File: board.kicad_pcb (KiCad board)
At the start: 2 copper layers, 96.3 x 46.3 mm, 38 parts, among them J0 Battery Pads, J1 Shard, J2 USB-Micro, SW0 RESET, SW1 UP, SW2 DOWN, SW3 LEFT, SW4 RIGHT, SW5 BTN_A, SW6 BTN_B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

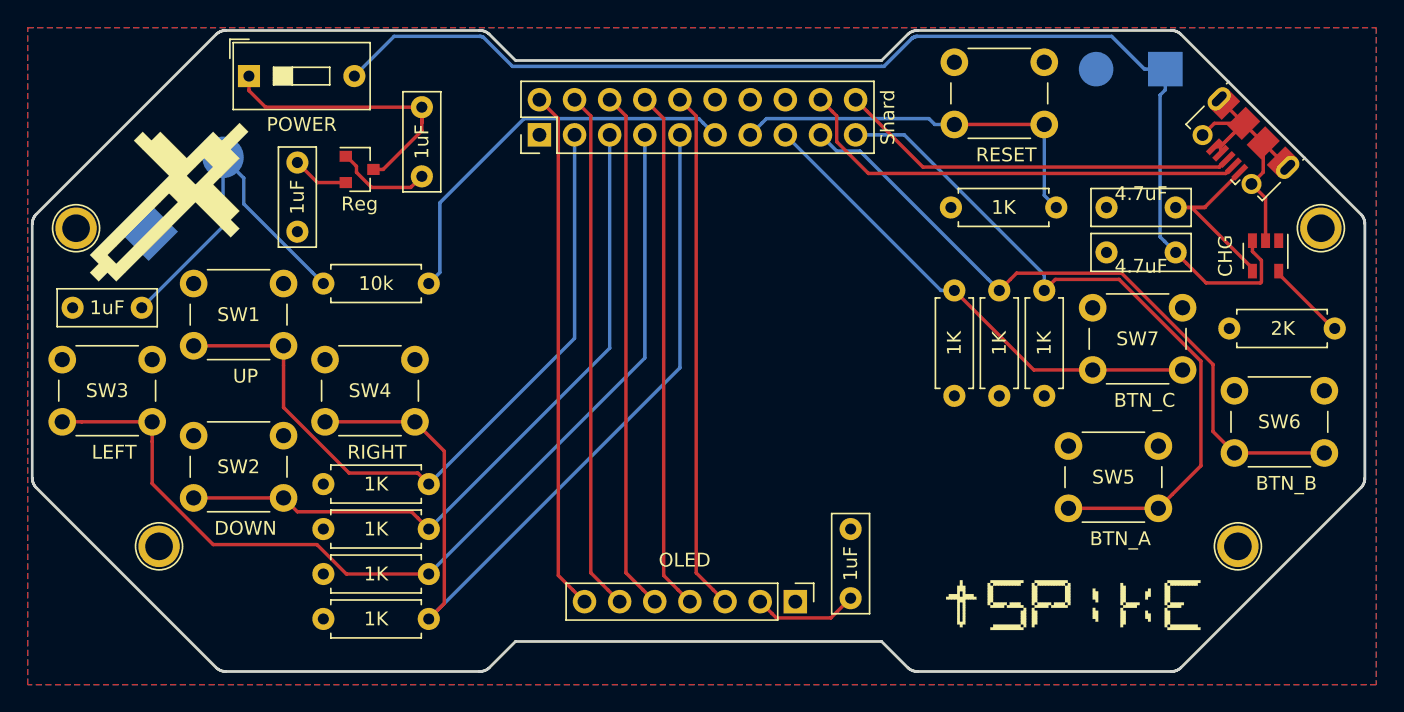
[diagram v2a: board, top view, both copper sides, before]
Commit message: board revised for mono oled
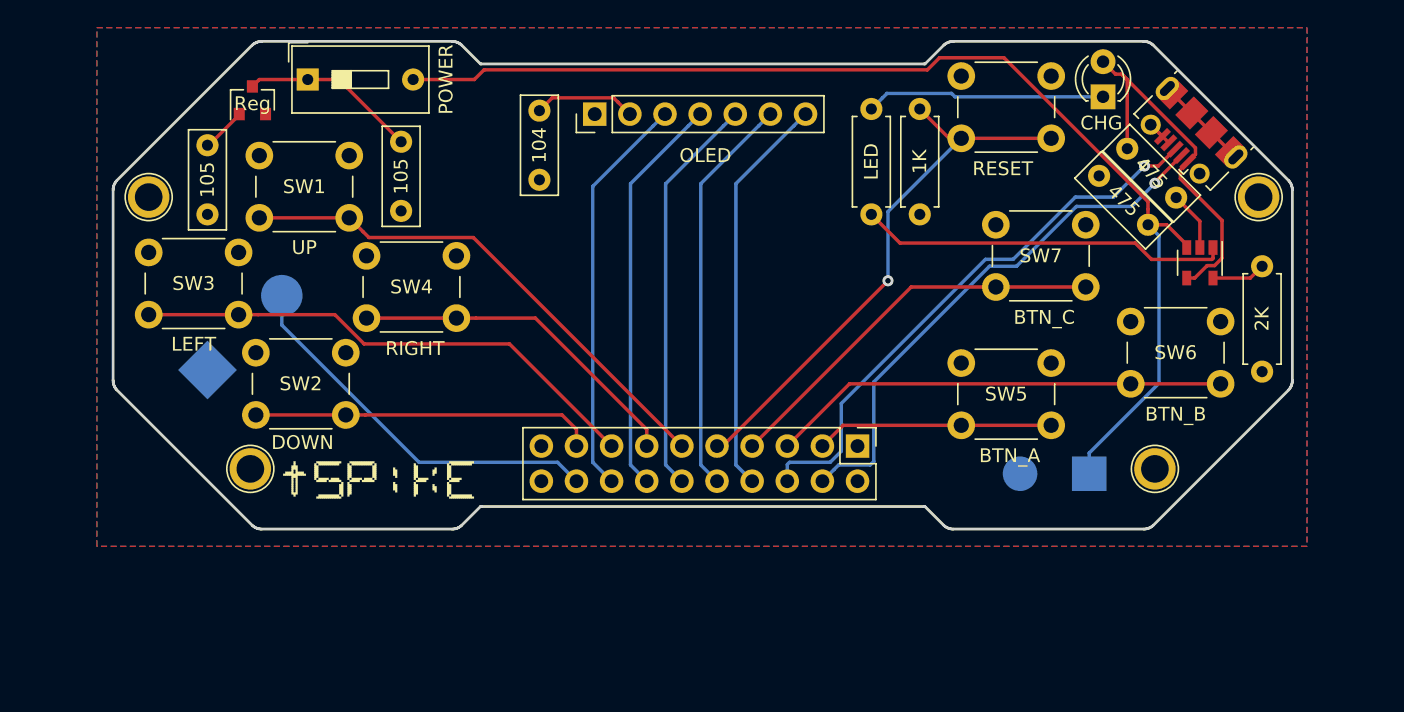
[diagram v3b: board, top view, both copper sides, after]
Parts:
- removed C4: 1uF, Capacitor_THT:C_Rect_L7.0mm_W2.5mm_P5.00mm
- removed R3, R4, R5, R6, R7: 1K, Resistor_THT:R_Axial_DIN0207_L6.3mm_D2.5mm_P7.62mm_Horizontal
- removed R8: 2K, Resistor_THT:R_Axial_DIN0207_L6.3mm_D2.5mm_P7.62mm_Horizontal
- removed R9: 10k, Resistor_THT:R_Axial_DIN0207_L6.3mm_D2.5mm_P7.62mm_Horizontal
- removed the REF** at (196.0, 97.0)
- removed the REF** at (106.0, 97.0)
- removed the REF** at (190.0, 120.0)
- removed the REF** at (112.0, 120.0)
- removed SPIKE: , SPIKE
- added D1: CHG, LED_THT:LED_D3.0mm, F.Cu at (180.2, 87.5)
- added REF**: TestPoint_Plated_Hole_D2.0mm, TestPoint:TestPoint_Plated_Hole_D2.0mm, F.Cu at (184.0, 114.4)
- added REF**: TestPoint_Plated_Hole_D2.0mm, TestPoint:TestPoint_Plated_Hole_D2.0mm, F.Cu at (111.2, 94.8)
- added REF**: TestPoint_Plated_Hole_D2.0mm, TestPoint:TestPoint_Plated_Hole_D2.0mm, F.Cu at (118.6, 114.4)
- added REF**: TestPoint_Plated_Hole_D2.0mm, TestPoint:TestPoint_Plated_Hole_D2.0mm, F.Cu at (191.5, 94.8)
- C1: value 1uF -> 104
- C2, C3: value 1uF -> 105
- C5, C6: value 4.7uF -> 475
- R1: value 1K -> LED
- R2: value 1K -> 2K
- U1: footprint Custom Footprints:128x128-OLED -> Custom Footprints:128x64-OLED
- U2: value CHG -> CHG CTRL
- moved R2 63.2 mm to (191.8, 99.8), turned to 270 degrees
- moved LOGO 48.6 mm to (120.7, 113.7)
- moved C1 41.8 mm to (139.5, 88.5), turned to 270 degrees
- moved U1 38.1 mm to (143.5, 88.8), turned to 90 degrees
- moved R1 37.5 mm to (163.5, 96.0), turned to 90 degrees
- moved J1 32.2 mm to (162.5, 112.8), turned to 270 degrees
- moved J0 29.8 mm to (176.8, 114.8)
- moved LS1 10.9 mm to (115.5, 107.2)
- moved SW1 10.4 mm to (119.2, 91.8)
- moved SW3 9.96 mm to (111.2, 98.8)
- moved SW5 9.80 mm to (170.0, 106.8)
- moved U3 9.22 mm to (118.8, 87.8), turned to 90 degrees
- moved SW7 9.22 mm to (172.5, 96.8)
- moved SW6 9.01 mm to (182.2, 103.8)
- moved SW4 8.08 mm to (127.0, 99.0)
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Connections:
- J1 pad 10: D_SCK -> D_DC
- J1 pad 11: SND -> UP
- J1 pad 12: GND -> D_RST
- J1 pad 13: RESET -> RIGHT
- J1 pad 14: GND -> D_MOSI
- J1 pad 15: BTN_C -> LEFT
- J1 pad 16: GND -> D_SCK
- J1 pad 17: BTN_B -> DOWN
- J1 pad 18: D- -> SND
- J1 pad 19: BTN_A -> GND
- J1 pad 2: D_CS -> GND
- J1 pad 20: D+ -> +3V3
- J1 pad 3: UP -> BTN_A
- J1 pad 4: D_DC -> D-
- J1 pad 5: DOWN -> BTN_B
- J1 pad 6: D_RST -> D+
- J1 pad 7: LEFT -> BTN_C
- J1 pad 8: D_MOSI -> D_CS
- J1 pad 9: RIGHT -> RESET
- LS1 pad 2: Net-(C4-Pad1) -> SND
- R1 pad 1: UP -> Net-(R1-Pad1)
- R1 pad 2: GND -> Net-(D1-Pad1)
- R2 pad 1: DOWN -> Net-(R2-Pad1)
- U2 pad 1: Net-(U2-Pad1) -> Net-(R1-Pad1)
- U2 pad 5: Net-(R8-Pad1) -> Net-(R2-Pad1)
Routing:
- net RIGHT: track 64.6 -> 24.8 mm
- net LEFT: track 71.9 -> 37.4 mm
- net BTN_A: track 51.5 -> 17.2 mm
- net DOWN: track 51.8 -> 24.8 mm
- net Net-(R1-Pad1): track 0.00 -> 26.9 mm
- net Net-(C4-Pad1): track 25.4 -> 0.00 mm
- net Net-(D1-Pad1): track 0.00 -> 17.3 mm
- net BTN_B: track 49.8 -> 33.2 mm
- net UP: track 53.4 -> 37.4 mm
- net CHARGE: track 14.3 -> 27.6 mm
- net GND: track 30.2 -> 17.0 mm
- net RESET: track 28.3 -> 40.2 mm, vias 0 -> 1
- net D+: track 29.1 -> 40.7 mm, vias 0 -> 1
- net D_DC: track 37.6 -> 29.1 mm
- net D_MOSI: track 37.6 -> 29.1 mm
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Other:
- board size 96.3 x 46.3 mm -> 85.3 x 35.3 mm

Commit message: swapped buttons to pull to GND
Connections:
- SW1 pad 1: +3V3 -> GND
- SW2 pad 1: +3V3 -> GND
- SW3 pad 1: +3V3 -> GND
- SW4 pad 1: +3V3 -> GND
- SW5 pad 1: +3V3 -> GND
- SW6 pad 1: +3V3 -> GND
- SW7 pad 1: +3V3 -> GND
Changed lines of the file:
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@@
     )
     (pad 1 thru_hole circle (at 6.5 0 90) (size 2 2) (drill 1.1) (layers *.Cu *.Mask)
-      (net 1 +3V3))
+      (net 2 GND))
     (pad 2 thru_hole circle (at 6.5 4.5 90) (size 2 2) (drill 1.1) (layers *.Cu *.Mask)
       (net 8 UP))
     (pad 1 thru_hole circle (at 0 0 90) (size 2 2) (drill 1.1) (layers *.Cu *.Mask)
-      (net 1 +3V3))
+      (net 2 GND))
     (pad 2 thru_hole circle (at 0 4.5 90) (size 2 2) (drill 1.1) (layers *.Cu *.Mask)
       (net 8 UP))
@@
       (net 9 DOWN))
     (pad 1 thru_hole circle (at 0 0 90) (size 2 2) (drill 1.1) (layers *.Cu *.Mask)
-      (net 1 +3V3))
+      (net 2 GND))
     (pad 2 thru_hole circle (at 6.5 4.5 90) (size 2 2) (drill 1.1) (layers *.Cu *.Mask)
       (net 9 DOWN))
     (pad 1 thru_hole circle (at 6.5 0 90) (size 2 2) (drill 1.1) (layers *.Cu *.Mask)
-      (net 1 +3V3))
+      (net 2 GND))
     (model ${KISYS3DMOD}/Button_Switch_THT.3dshapes/SW_PUSH_6mm.wrl
       (at (xyz 0 0 0))
@@
     )
     (pad 1 thru_hole circle (at 6.5 0 90) (size 2 2) (drill 1.1) (layers *.Cu *.Mask)
-      (net 1 +3V3))
+      (net 2 GND))
     (pad 2 thru_hole circle (at 6.5 4.5 90) (size 2 2) (drill 1.1) (layers *.Cu *.Mask)
       (net 10 LEFT))
     (pad 1 thru_hole circle (at 0 0 90) (size 2 2) (drill 1.1) (layers *.Cu *.Mask)
-      (net 1 +3V3))
+      (net 2 GND))
     (pad 2 thru_hole circle (at 0 4.5 90) (size 2 2) (drill 1.1) (layers *.Cu *.Mask)
       (net 10 LEFT))
@@
       (net 11 RIGHT))
     (pad 1 thru_hole circle (at 0 0 90) (size 2 2) (drill 1.1) (layers *.Cu *.Mask)
-      (net 1 +3V3))
+      (net 2 GND))
     (pad 2 thru_hole circle (at 6.5 4.5 90) (size 2 2) (drill 1.1) (layers *.Cu *.Mask)
       (net 11 RIGHT))
     (pad 1 thru_hole circle (at 6.5 0 90) (size 2 2) (drill 1.1) (layers *.Cu *.Mask)
-      (net 1 +3V3))
+      (net 2 GND))
     (model ${KISYS3DMOD}/Button_Switch_THT.3dshapes/SW_PUSH_6mm.wrl
       (at (xyz 0 0 0))
@@
     )
     (pad 1 thru_hole circle (at 6.5 0 90) (size 2 2) (drill 1.1) (layers *.Cu *.Mask)
-      (net 1 +3V3))
+      (net 2 GND))
     (pad 2 thru_hole circle (at 6.5 4.5 90) (size 2 2) (drill 1.1) (layers *.Cu *.Mask)
       (net 12 BTN_A))
     (pad 1 thru_hole circle (at 0 0 90) (size 2 2) (drill 1.1) (layers *.Cu *.Mask)
-      (net 1 +3V3))
+      (net 2 GND))
     (pad 2 thru_hole circle (at 0 4.5 90) (size 2 2) (drill 1.1) (layers *.Cu *.Mask)
       (net 12 BTN_A))
@@
       (net 13 BTN_B))
     (pad 1 thru_hole circle (at 0 0 90) (size 2 2) (drill 1.1) (layers *.Cu *.Mask)
-      (net 1 +3V3))
+      (net 2 GND))
     (pad 2 thru_hole circle (at 6.5 4.5 90) (size 2 2) (drill 1.1) (layers *.Cu *.Mask)
       (net 13 BTN_B))
     (pad 1 thru_hole circle (at 6.5 0 90) (size 2 2) (drill 1.1) (layers *.Cu *.Mask)
-      (net 1 +3V3))
+      (net 2 GND))
     (model ${KISYS3DMOD}/Button_Switch_THT.3dshapes/SW_PUSH_6mm.wrl
       (at (xyz 0 0 0))
@@
     )
     (pad 1 thru_hole circle (at 6.5 0 90) (size 2 2) (drill 1.1) (layers *.Cu *.Mask)
-      (net 1 +3V3))
+      (net 2 GND))
     (pad 2 thru_hole circle (at 6.5 4.5 90) (size 2 2) (drill 1.1) (layers *.Cu *.Mask)
       (net 14 BTN_C))
     (pad 1 thru_hole circle (at 0 0 90) (size 2 2) (drill 1.1) (layers *.Cu *.Mask)
-      (net 1 +3V3))
+      (net 2 GND))
     (pad 2 thru_hole circle (at 0 4.5 90) (size 2 2) (drill 1.1) (layers *.Cu *.Mask)
       (net 14 BTN_C))
@@
   (gr_line (start 167.3735 85.1265) (end 167.3074 85.123) (layer Edge.Cuts) (width 0.2))
   (gr_line (start 168.75 83.75) (end 167.3735 85.1265) (layer Edge.Cuts) (width 0.2))
-  (via (at 164.7 100.8) (size 0.8) (drill 0.4) (layers F.Cu B.Cu) (net 6))
   (segment (start 144.864999 87.574999) (end 145.190001 87.900001) (width 0.25) (layer F.Cu) (net 1))
   (segment (start 145.190001 87.900001) (end 146.04 88.75) (width 0.25) (layer F.Cu) (net 1))
   (segment (start 140.425001 87.574999) (end 144.864999 87.574999) (width 0.25) (layer F.Cu) (net 1))
   (segment (start 139.5 88.5) (end 140.425001 87.574999) (width 0.25) (layer F.Cu) (net 1))
-  (via (at 183.25 92.5) (size 0.8) (drill 0.4) (layers F.Cu B.Cu) (net 20))
-  (via (at 184 93.75) (size 0.8) (drill 0.4) (layers F.Cu B.Cu) (net 21))
   (segment (start 188.082151 90.082062) (end 189.849918 91.849829) (width 0.25) (layer F.Cu) (net 2))
   (segment (start 185.324435 87.324346) (end 186.667938 88.667849) (width 0.25) (layer F.Cu) (net 2))
@@
   (segment (start 183.5 95.61863) (end 183.5 96.75) (width 0.25) (layer F.Cu) (net 5))
   (segment (start 167.549546 85.551508) (end 168.426055 84.674999) (width 0.25) (layer F.Cu) (net 5))
+  (via (at 164.7 100.8) (size 0.8) (drill 0.4) (layers F.Cu B.Cu) (net 6))
   (segment (start 169.12 90.5) (end 170 90.5) (width 0.25) (layer F.Cu) (net 6))
   (segment (start 167 88.38) (end 169.12 90.5) (width 0.25) (layer F.Cu) (net 6))
@@
   (segment (start 143.355001 93.974999) (end 147.730001 89.599999) (width 0.25) (layer B.Cu) (net 19))
   (segment (start 144.72 115.29) (end 143.355001 113.925001) (width 0.25) (layer B.Cu) (net 19))
+  (via (at 183.25 92.5) (size 0.8) (drill 0.4) (layers F.Cu B.Cu) (net 20))
   (segment (start 184.25 92.5) (end 183.25 92.5) (width 0.25) (layer F.Cu) (net 20))
   (segment (start 185.465856 91.284144) (end 184.25 92.5) (width 0.25) (layer F.Cu) (net 20))
@@
   (segment (start 181 94.75) (end 183.25 92.5) (width 0.25) (layer B.Cu) (net 20))
   (segment (start 178.25 94.75) (end 181 94.75) (width 0.25) (layer B.Cu) (net 20))
+  (via (at 184 93.75) (size 0.8) (drill 0.4) (layers F.Cu B.Cu) (net 21))
   (segment (start 184 93.669239) (end 184 93.75) (width 0.25) (layer F.Cu) (net 21))
   (segment (start 185.925476 91.743763) (end 184 93.669239) (width 0.25) (layer F.Cu) (net 21))

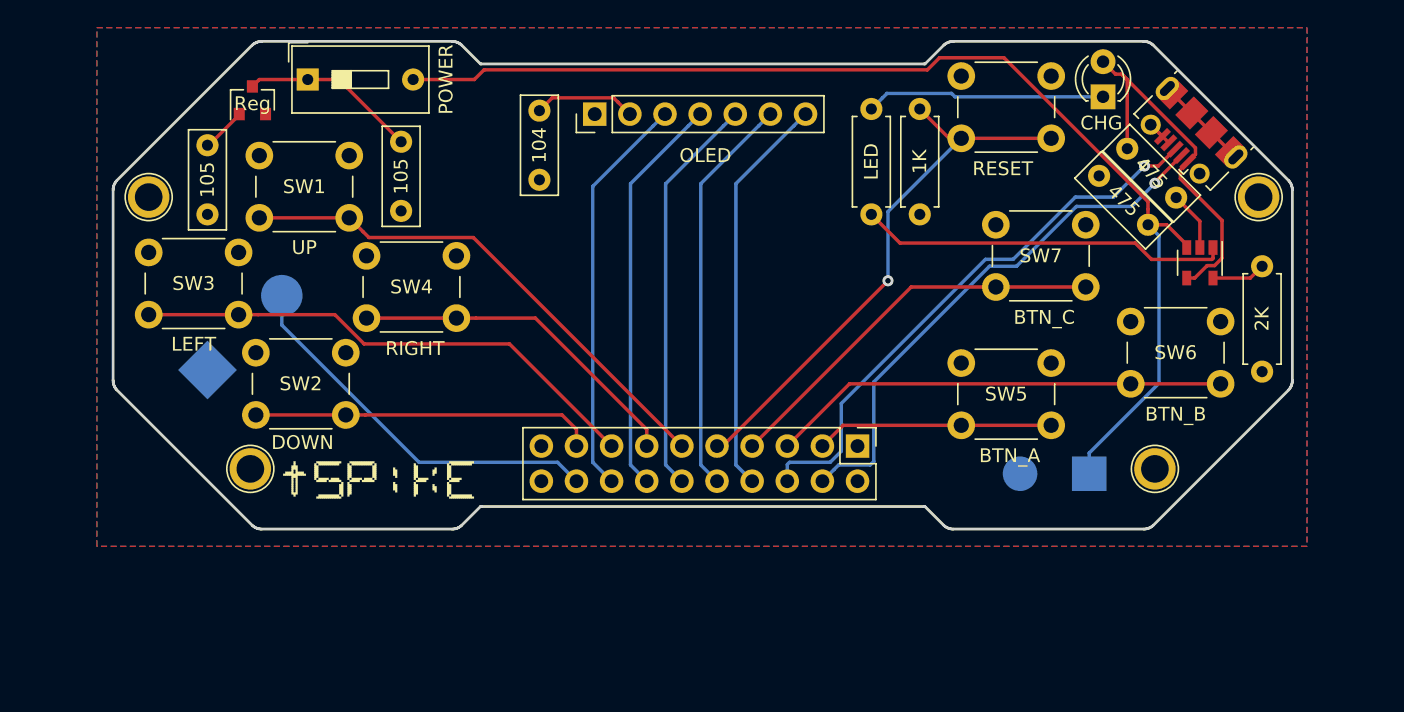
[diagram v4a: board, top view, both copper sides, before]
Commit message: Edge Connector for Shards
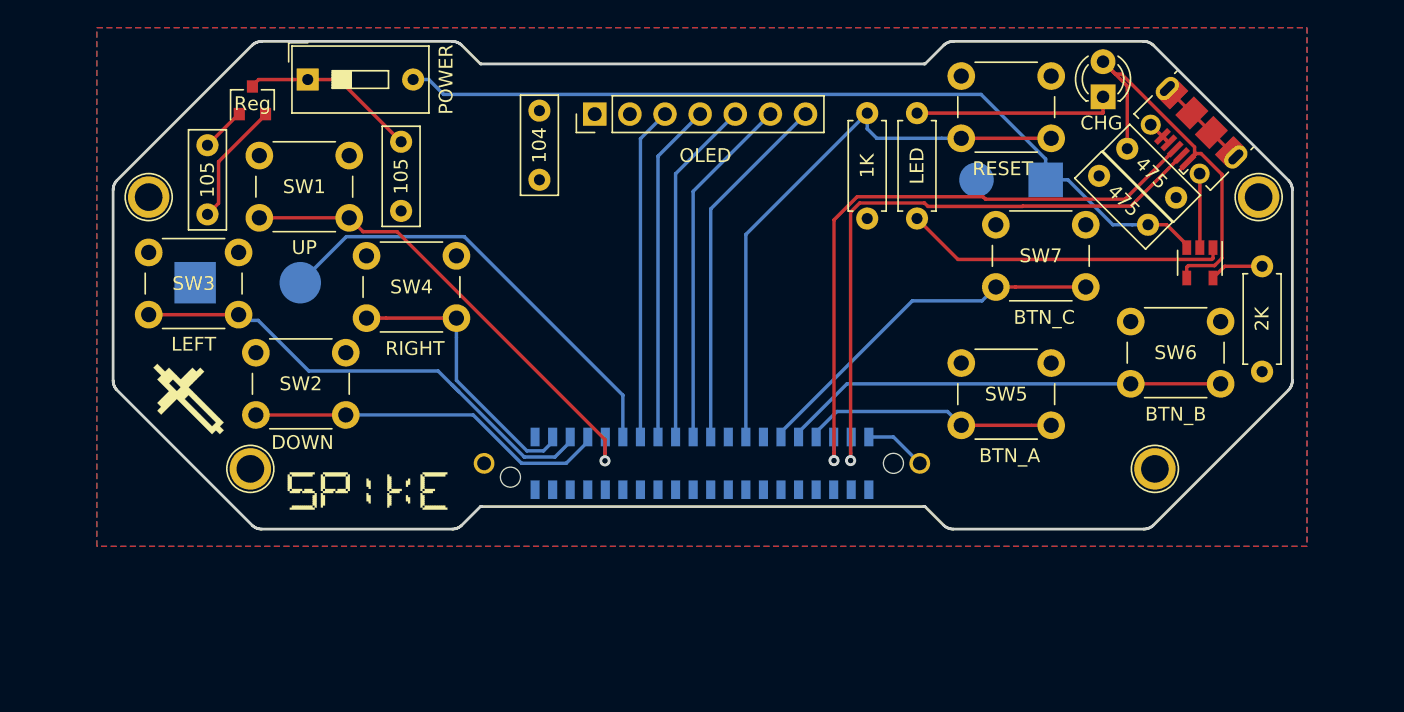
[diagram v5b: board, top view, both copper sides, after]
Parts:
- added SPIKE: , SPIKE, F.Cu at (109.8, 108.5)
- added SPIKE: , SPIKE, B.Cu at (162.2, 98.0)
- J1: footprint Connector_PinHeader_2.54mm:PinHeader_2x10_P2.54mm_Vertical -> Connector_PCBEdge:Samtec_MECF-20-01-NP-L-DV-WT_2x20_P1.27mm_Socket_Horizontal; moved to B.Cu
- moved J0 21.5 mm to (173.6, 93.5)
- moved J1 11.3 mm to (151.2, 114.0), turned to 180 degrees
- moved LS1 6.37 mm to (114.6, 100.9), turned to 0 degrees
- moved R0 3.81 mm to (163.2, 96.3)
- moved R1 3.31 mm to (166.8, 96.3)
- moved LOGO 0.99 mm to (121.2, 114.5)
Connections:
- J1 pad 1: +3V3 -> Net-(J1-Pad1)
- J1 pad 10: D_DC -> BTN_B
- J1 pad 11: UP -> Net-(J1-Pad11)
- J1 pad 12: D_RST -> BTN_C
- J1 pad 13: RIGHT -> Net-(J1-Pad13)
- J1 pad 14: D_MOSI -> Net-(J1-Pad14)
- J1 pad 15: LEFT -> Net-(J1-Pad15)
- J1 pad 16: D_SCK -> RESET
- J1 pad 17: DOWN -> Net-(J1-Pad17)
- J1 pad 18: SND -> Net-(J1-Pad18)
- J1 pad 19: GND -> Net-(J1-Pad19)
- J1 pad 2: GND -> +3V3
- J1 pad 20: +3V3 -> D_CS
- J1 pad 3: BTN_A -> Net-(J1-Pad3)
- J1 pad 5: BTN_B -> Net-(J1-Pad5)
- J1 pad 7: BTN_C -> Net-(J1-Pad7)
- J1 pad 8: D_CS -> BTN_A
- J1 pad 9: RESET -> Net-(J1-Pad9)
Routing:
- net +BATT: track 83.8 -> 62.0 mm
- net D-: track 39.1 -> 45.5 mm
- net +3V3: track 7.41 -> 13.5 mm
- net D+: track 40.7 -> 46.0 mm
- net D_SCK: track 29.3 -> 24.1 mm
- net SND: track 28.1 -> 32.8 mm
- net CHARGE: track 27.6 -> 31.9 mm
- net D_MOSI: track 29.1 -> 25.0 mm
- net RIGHT: track 24.8 -> 20.7 mm
- net D_RST: track 29.1 -> 25.5 mm
- net Net-(R1-Pad1): track 26.9 -> 23.4 mm
- net D_DC: track 29.1 -> 26.0 mm
- net D_CS: track 29.1 -> 26.2 mm
- net Net-(D1-Pad1): track 17.3 -> 14.6 mm
- net RESET: track 40.2 -> 42.6 mm, vias 1 -> 0
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
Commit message: Board updated to edge connector
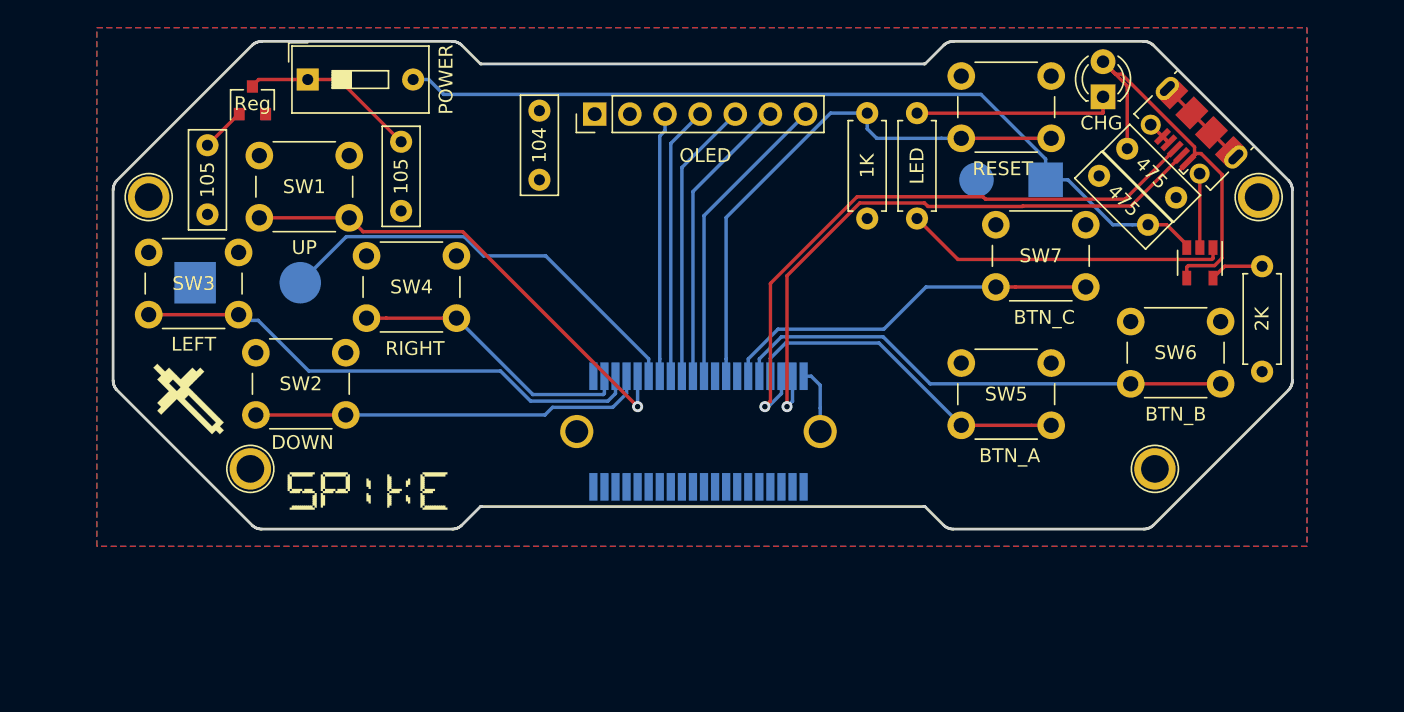
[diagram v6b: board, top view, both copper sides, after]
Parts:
- J1: footprint Connector_PCBEdge:Samtec_MECF-20-01-NP-L-DV-WT_2x20_P1.27mm_Socket_Horizontal -> Custom Footprints:Samtec_MEC8-120-02-L-D-RA1_Socket
- moved J1 7.70 mm to (158.6, 111.7)
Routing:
- net +3V3: track 13.5 -> 5.25 mm
- net BTN_A: track 18.4 -> 24.5 mm
- net D_MOSI: track 25.0 -> 19.8 mm
- net D_SCK: track 24.1 -> 19.1 mm
- net D_RST: track 25.5 -> 20.5 mm
- net D_DC: track 26.0 -> 21.3 mm
- net BTN_B: track 32.3 -> 36.7 mm
- net D_CS: track 26.2 -> 22.0 mm
- net DOWN: track 26.4 -> 28.7 mm
- net RESET: track 42.6 -> 40.4 mm
- net D-: track 45.5 -> 44.2 mm
- net SND: track 32.8 -> 31.5 mm
- net LEFT: track 36.6 -> 37.8 mm
- net BTN_C: track 26.7 -> 27.8 mm
- net D+: track 46.0 -> 45.3 mm
